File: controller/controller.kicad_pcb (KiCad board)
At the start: 4 copper layers, 30 x 60 mm, 74 parts, among them SW1 SW_SPDT, SW2 SW_SPST

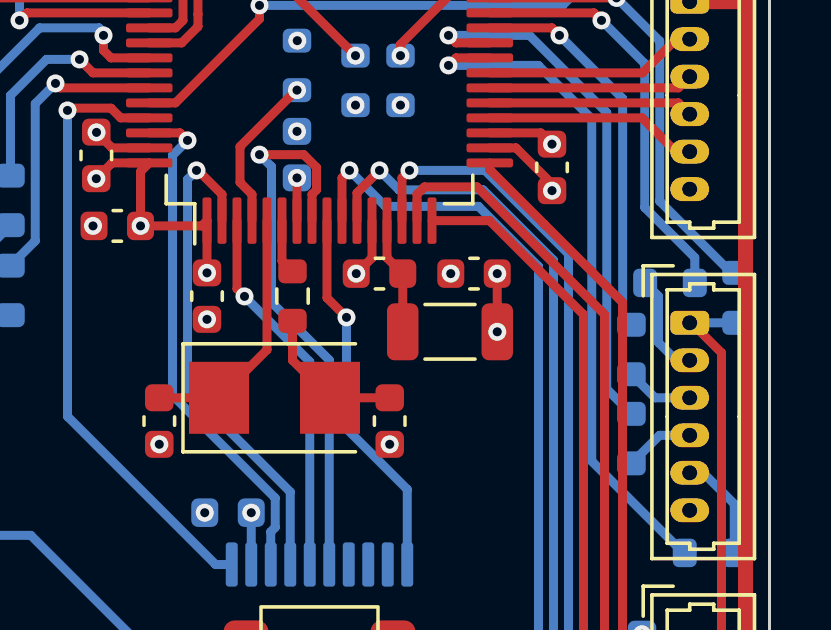
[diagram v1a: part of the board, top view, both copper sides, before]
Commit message: start work on host mcu
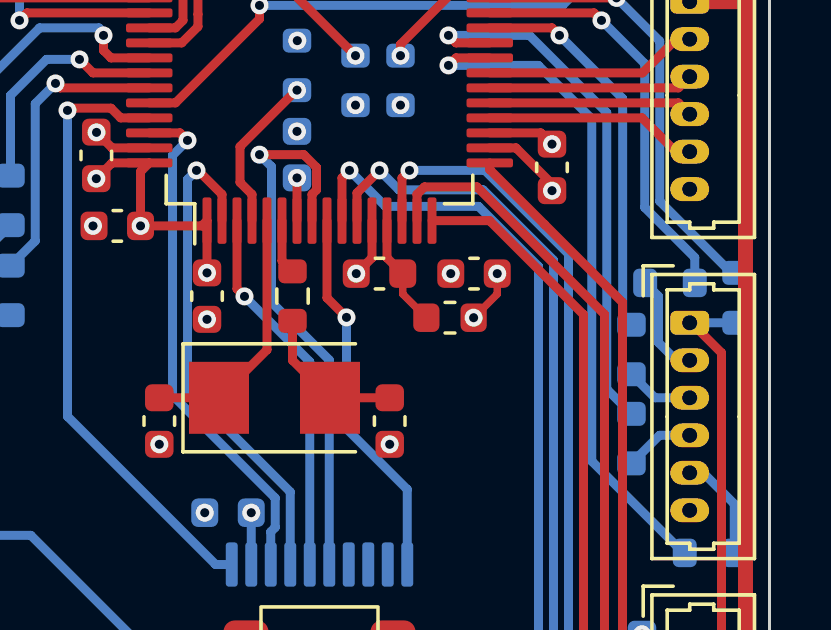
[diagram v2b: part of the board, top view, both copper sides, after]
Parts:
- FB1: footprint Inductor_SMD:L_1206_3216Metric -> Inductor_SMD:L_0603_1608Metric
- moved FB1 0.47 mm to (129.3, 79.9)
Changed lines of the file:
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@@
     )
   )
-  (footprint "Inductor_SMD:L_1206_3216Metric" (layer "F.Cu")
-    (at 129.35 80.38 180)
-    (descr "Inductor SMD 1206 (3216 Metric), square (rectangular) end terminal, IPC_7351 nominal, (Body size source: IPC-SM-782 page 80, https://www.pcb-3d.com/wordpress/wp-content/uploads/ipc-sm-782a_amendment_1_and_2.pdf), generated with kicad-footprint-generator")
+  (footprint "Inductor_SMD:L_0603_1608Metric" (layer "F.Cu")
+    (at 129.35 79.91 180)
+    (descr "Inductor SMD 0603 (1608 Metric), square (rectangular) end terminal, IPC_7351 nominal, (Body size source: http://www.tortai-tech.com/upload/download/2011102023233369053.pdf), generated with kicad-footprint-generator")
     (tags "inductor")
     (property "Sheetfile" "controller.kicad_sch")
     (property "Sheetname" "")
     (attr smd)
-    (fp_text reference "FB1" (at 0 -1.9) (layer "F.Fab")
+    (fp_text reference "FB1" (at 0 -1.43 180) (layer "F.Fab")
       (effects (font (size 1 1) (thickness 0.15)))
     )
-    (fp_text value "120R" (at 0 1.9) (layer "F.Fab")
+    (fp_text value "120R" (at 0 1.43 180) (layer "F.Fab")
       (effects (font (size 1 1) (thickness 0.15)))
     )
-    (fp_text user "${REFERENCE}" (at 0 0) (layer "F.Fab")
-      (effects (font (size 0.8 0.8) (thickness 0.12)))
+    (fp_text user "${REFERENCE}" (at 0 0 180) (layer "F.Fab")
+      (effects (font (size 0.4 0.4) (thickness 0.06)))
     )
-    (fp_line (start -0.835242 0.91) (end 0.835242 0.91) (layer "F.SilkS") (width 0.12))
-    (fp_line (start -0.835242 -0.91) (end 0.835242 -0.91) (layer "F.SilkS") (width 0.12))
-    (fp_line (start 2.35 -1.2) (end 2.35 1.2) (layer "F.CrtYd") (width 0.05))
-    (fp_line (start 2.35 1.2) (end -2.35 1.2) (layer "F.CrtYd") (width 0.05))
-    (fp_line (start -2.35 -1.2) (end 2.35 -1.2) (layer "F.CrtYd") (width 0.05))
-    (fp_line (start -2.35 1.2) (end -2.35 -1.2) (layer "F.CrtYd") (width 0.05))
-    (fp_line (start -1.6 0.8) (end -1.6 -0.8) (layer "F.Fab") (width 0.1))
-    (fp_line (start 1.6 0.8) (end -1.6 0.8) (layer "F.Fab") (width 0.1))
-    (fp_line (start -1.6 -0.8) (end 1.6 -0.8) (layer "F.Fab") (width 0.1))
-    (fp_line (start 1.6 -0.8) (end 1.6 0.8) (layer "F.Fab") (width 0.1))
-    (pad "1" smd roundrect (at -1.575 0 180) (size 1.05 1.9) (layers "F.Cu" "F.Paste" "F.Mask") (roundrect_rratio 0.238095)
+    (fp_line (start -0.162779 -0.51) (end 0.162779 -0.51) (layer "F.SilkS") (width 0.12))
+    (fp_line (start -0.162779 0.51) (end 0.162779 0.51) (layer "F.SilkS") (width 0.12))
+    (fp_line (start -1.48 -0.73) (end 1.48 -0.73) (layer "F.CrtYd") (width 0.05))
+    (fp_line (start 1.48 -0.73) (end 1.48 0.73) (layer "F.CrtYd") (width 0.05))
+    (fp_line (start 1.48 0.73) (end -1.48 0.73) (layer "F.CrtYd") (width 0.05))
+    (fp_line (start -1.48 0.73) (end -1.48 -0.73) (layer "F.CrtYd") (width 0.05))
+    (fp_line (start -0.8 0.4) (end -0.8 -0.4) (layer "F.Fab") (width 0.1))
+    (fp_line (start 0.8 -0.4) (end 0.8 0.4) (layer "F.Fab") (width 0.1))
+    (fp_line (start 0.8 0.4) (end -0.8 0.4) (layer "F.Fab") (width 0.1))
+    (fp_line (start -0.8 -0.4) (end 0.8 -0.4) (layer "F.Fab") (width 0.1))
+    (pad "1" smd roundrect (at -0.7875 0 180) (size 0.875 0.95) (layers "F.Cu" "F.Paste" "F.Mask") (roundrect_rratio 0.25)
       (net 3 "+3V3") (pintype "passive"))
-    (pad "2" smd roundrect (at 1.575 0 180) (size 1.05 1.9) (layers "F.Cu" "F.Paste" "F.Mask") (roundrect_rratio 0.238095)
+    (pad "2" smd roundrect (at 0.7875 0 180) (size 0.875 0.95) (layers "F.Cu" "F.Paste" "F.Mask") (roundrect_rratio 0.25)
       (net 4 "+3.3VA") (pintype "passive"))
-    (model "${KICAD6_3DMODEL_DIR}/Inductor_SMD.3dshapes/L_1206_3216Metric.wrl"
+    (model "${KICAD6_3DMODEL_DIR}/Inductor_SMD.3dshapes/L_0603_1608Metric.wrl"
       (offset (xyz 0 0 0))
       (scale (xyz 1 1 1))
@@
   (segment (start 131.915 67.25) (end 132.4325 66.7325) (width 0.3) (layer "F.Cu") (net 3))
   (segment (start 130.0375 60.05) (end 131 60.05) (width 0.3) (layer "F.Cu") (net 3))
+  (segment (start 130.925 78.44) (end 130.925 79.1225) (width 0.25) (layer "F.Cu") (net 3))
+  (segment (start 130.925 79.1225) (end 130.1375 79.91) (width 0.25) (layer "F.Cu") (net 3))
   (segment (start 119.035 75.04) (end 119.325 74.75) (width 0.3) (layer "F.Cu") (net 3))
   (segment (start 132.375 73.75) (end 132.7375 74.1125) (width 0.3) (layer "F.Cu") (net 3))
@@
   (segment (start 119.035 76.85) (end 119.035 75.04) (width 0.3) (layer "F.Cu") (net 3))
   (segment (start 121.25 76.675) (end 121.25 78.415) (width 0.3) (layer "F.Cu") (net 3))
-  (segment (start 130.925 79.475) (end 130.925 80.38) (width 0.3) (layer "F.Cu") (net 3))
   (segment (start 132.7375 74.1125) (end 132.75 74.125) (width 0.3) (layer "F.Cu") (net 3))
-  (segment (start 130.925 78.44) (end 130.925 79.475) (width 0.3) (layer "F.Cu") (net 3))
   (segment (start 121.25 65.325) (end 120.4 65.325) (width 0.3) (layer "F.Cu") (net 3))
   (via (at 121.25 78.415) (size 0.6) (drill 0.3) (layers "F.Cu" "B.Cu") (net 3))
@@
   (via (at 119.035 76.85) (size 0.6) (drill 0.3) (layers "F.Cu" "B.Cu") (net 3))
   (via (at 131.76 60.05) (size 0.6) (drill 0.3) (layers "F.Cu" "B.Cu") (net 3))
-  (via (at 130.925 80.38) (size 0.6) (drill 0.3) (layers "F.Cu" "B.Cu") (net 3))
+  (via (at 130.1375 79.91) (size 0.6) (drill 0.3) (layers "F.Cu" "B.Cu") (net 3))
   (via (at 132.44 66.725) (size 0.6) (drill 0.3) (layers "F.Cu" "B.Cu") (net 3))
   (via (at 117.56 75.275) (size 0.6) (drill 0.3) (layers "F.Cu" "B.Cu") (net 3))
@@
   (segment (start 127.25 77.915) (end 127.775 78.44) (width 0.3) (layer "F.Cu") (net 4))
   (segment (start 127.25 76.675) (end 127.25 77.915) (width 0.3) (layer "F.Cu") (net 4))
-  (segment (start 127.775 78.44) (end 127.775 80.38) (width 0.3) (layer "F.Cu") (net 4))
+  (segment (start 127.775 78.44) (end 127.775 79.1225) (width 0.25) (layer "F.Cu") (net 4))
+  (segment (start 127.775 79.1225) (end 128.5625 79.91) (width 0.25) (layer "F.Cu") (net 4))
   (segment (start 130.675 68.25) (end 129.25 68.25) (width 0.3) (layer "F.Cu") (net 5))
   (via (at 129.25 68.25) (size 0.6) (drill 0.3) (layers "F.Cu" "B.Cu") (net 5))

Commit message: update controller and host boards
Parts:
- removed ESD1: USBLC6-2SC6, Package_TO_SOT_SMD:SOT-23-6
- removed H10, H11, H12, H13, H14: Conn_01x03, Connector_Molex:Molex_PicoBlade_53047-0310_1x03_P1.25mm_Vertical
- removed H2, H4, H5, H6: Conn_01x06, Connector_Molex:Molex_PicoBlade_53047-0610_1x06_P1.25mm_Vertical
- removed H3, H8, H9: Conn_01x05, Connector_Molex:Molex_PicoBlade_53047-0510_1x05_P1.25mm_Vertical
- removed H7: Conn_01x04, Connector_Molex:Molex_PicoBlade_53047-0410_1x04_P1.25mm_Vertical
- removed LDO1: AP2127N-3.3, Package_TO_SOT_SMD:SOT-23
- removed MCU1: STM32F401RCT6, Package_QFP:LQFP-64_10x10mm_P0.5mm
- removed MNT1: MountingHole, MountingHole:MountingHole_2.2mm_M2_Pad
- removed R10, R11, R12, R13, R14, R15, R16, R17, R18, R19, R20, R21, R22, R23, R24, R25, R26, R27, R28, R29, R5, R6, R7, R8, R9: 10KR, Resistor_SMD:R_0603_1608Metric
- removed SW2: SW_SPST, Custom:ALPS_SKRKAEE020
- removed USB1: USB_A, Custom:JST_UBA-4R-D14T-4D
- removed VT1: TXS0108EPW, Package_SO:TSSOP-20_4.4x6.5mm_P0.65mm
- removed XTAL1: 8MHz, Crystal:Crystal_SMD_5032-2Pin_5.0x3.2mm
- added J1: Conn_01x02, klib:MOLEX_533750210-Mini-Lock-2Pin-Through-Hole, F.Cu at (135.7, 74.0)
- added J10: Conn_01x05, Connector_Molex:Molex_PicoBlade_53047-0510_1x05_P1.25mm_Vertical, F.Cu at (137.3, 107.5)
- added J11: Conn_01x02, klib:MOLEX_533750210-Mini-Lock-2Pin-Through-Hole, F.Cu at (135.7, 126.0)
- added J2: USB_C_Receptacle_USB2.0, Connector_USB:USB_C_Receptacle_HRO_TYPE-C-31-M-12, F.Cu at (125.0, 73.0)
- added J3: Conn_01x02, klib:MOLEX_533750210-Mini-Lock-2Pin-Through-Hole, F.Cu at (114.3, 126.0)
- added J4: Conn_01x05, Connector_Molex:Molex_PicoBlade_53047-0510_1x05_P1.25mm_Vertical, F.Cu at (127.5, 127.3)
- added J5: Conn_01x04, Connector_Molex:Molex_PicoBlade_53047-0410_1x04_P1.25mm_Vertical, F.Cu at (112.7, 94.5)
- added J6: Conn_01x04, Connector_Molex:Molex_PicoBlade_53047-0410_1x04_P1.25mm_Vertical, F.Cu at (137.3, 92.5)
- added J7: Conn_01x05, Connector_Molex:Molex_PicoBlade_53047-0510_1x05_P1.25mm_Vertical, F.Cu at (112.7, 85.8)
- added J8: Conn_01x05, Connector_Molex:Molex_PicoBlade_53047-0510_1x05_P1.25mm_Vertical, F.Cu at (137.3, 82.5)
- added J9: Conn_01x05, Connector_Molex:Molex_PicoBlade_53047-0510_1x05_P1.25mm_Vertical, F.Cu at (112.7, 110.8)
- added U1: AP2127N-3.3, Package_TO_SOT_SMD:SOT-23, F.Cu at (131.2, 81.2)
- added U2: STM32F401RCT6, Package_QFP:LQFP-64_10x10mm_P0.5mm, F.Cu at (125.0, 94.0)
- added U3: USBLC6-2SC6, Package_TO_SOT_SMD:SOT-23-6, F.Cu at (123.0, 82.0)
- added U4: TXS0108EPW, Package_SO:TSSOP-20_4.4x6.5mm_P0.65mm, F.Cu at (125.0, 120.0)
- added Y1: 8M, Crystal:Crystal_SMD_5032-2Pin_5.0x3.2mm, F.Cu at (123.5, 106.5)
- C1, C2, C3, C9: value 10uF -> 10u
- C10, C4, C5, C6, C7, C8: value 100nF -> 100n
- C11: value 4.7uF -> 20p; moved to F.Cu
- C12: value 100nF -> 20p; moved to F.Cu
- C13: value 20pF -> 4.7u
- C14: value 20pF -> 100n
- C15, C16, C17, C18, C19, C20, C21: value 100nF -> 100n; moved to F.Cu
- H1: value Conn_01x06 -> MountingHole; footprint Connector_Molex:Molex_PicoBlade_53047-0610_1x06_P1.25mm_Vertical -> MountingHole:MountingHole_2.2mm_M2_Pad
- R1: value 0R -> 0
- R2, R3, R4: value 10KR -> 10K; moved to F.Cu
- SW1: footprint Custom:ALPS_SSSS912000 -> klib:ALPS_SSSS912000
- moved SW1 65.4 mm to (125.0, 113.0), turned to 180 degrees
- moved R4 53.4 mm to (134.8, 112.5)
- moved R2 44.7 mm to (125.0, 109.5), turned to 180 degrees
- moved C11 38.1 mm to (119.5, 105.3), turned to 90 degrees
- moved C15 33.0 mm to (119.5, 120.0), turned to 180 degrees
- moved C12 31.0 mm to (127.4, 105.3), turned to 90 degrees
- moved C16 26.2 mm to (130.5, 120.0), turned to 0 degrees
- moved C20 24.7 mm to (134.8, 107.5), turned to 90 degrees
- moved C9 23.8 mm to (130.4, 102.2), turned to 90 degrees
- moved R1 23.8 mm to (124.2, 103.0), turned to -90 degrees
- moved H1 23.8 mm to (114.0, 74.0), turned to 0 degrees
- moved FB1 23.1 mm to (128.1, 103.0)
- moved C5 23.1 mm to (132.5, 98.0)
- moved C10 23.1 mm to (128.1, 101.5), turned to 0 degrees
- moved C17 23.1 mm to (115.2, 105.8), turned to 90 degrees
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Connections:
- net +3.3VA renamed VREF
- C1 pad 1: VBUS -> 5V
- C11 pad 1: VCAP -> HSE_IN
- C12 pad 1: GND -> Net-(C12-Pad1)
- C12 pad 2: NRST -> GND
- C13 pad 1: HSE_IN -> VCAP
- C14 pad 1: Net-(C14-Pad1) -> NRST
- C15 pad 1: ST_X -> 3V3
- C16 pad 1: ST_Y -> 5V
- C2 pad 1: +3V3 -> 3V3
- C20 pad 1: GND -> ST_X
- C20 pad 2: +3V3 -> GND
- C21 pad 1: GND -> ST_Y
- C21 pad 2: VBUS -> GND
- C3 pad 1: +3V3 -> 3V3
- C4 pad 1: +3V3 -> 3V3
- C5 pad 1: +3V3 -> 3V3
- C6 pad 1: +3V3 -> 3V3
- C7 pad 1: +3V3 -> 3V3
- C8 pad 1: +3V3 -> 3V3
- C9 pad 1: +3V3 -> 3V3
- FB1 pad 1: +3V3 -> 3V3
- H1 pad 1: VBUS -> (no net)
- R1 pad 1: Net-(C14-Pad1) -> HSE_OUT
- R1 pad 2: HSE_OUT -> Net-(C12-Pad1)
- R2 pad 1: BOOT0 -> Net-(R2-Pad1)
- R2 pad 2: Net-(R2-Pad2) -> BOOT0
- R3 pad 1: BOOT1/KR1 -> BOOT1
- R3 pad 2: KR1 -> GND
- R4 pad 1: KT1 -> ST_P_IN
- R4 pad 2: KT1_IN -> ST_P
- SW1 pad 2: Net-(R2-Pad2) -> Net-(R2-Pad1)
- SW1 pad 3: +3V3 -> 3V3
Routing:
- net 5V: track 0.00 -> 145.5 mm, vias 0 -> 2
- net VBUS: track 131.6 -> 0.00 mm, vias 1 -> 0
- net 3V3: track 0.00 -> 70.4 mm, vias 0 -> 21
- net KR1: track 31.7 -> 0.00 mm
- net KI5: track 27.9 -> 0.00 mm, vias 1 -> 0
- net GND: track 12.6 -> 38.7 mm, vias 29 -> 33
- net KI1: track 26.1 -> 0.00 mm, vias 1 -> 0
- net LED4: track 12.5 -> 38.3 mm, vias 1 -> 2
- net KI2: track 24.8 -> 0.00 mm, vias 1 -> 0
- net KI4: track 23.3 -> 0.00 mm, vias 1 -> 0
- net KR5: track 22.8 -> 0.00 mm, vias 1 -> 0
- net KI3: track 22.4 -> 0.00 mm, vias 1 -> 0
- net LED_OE: track 12.6 -> 34.1 mm, vias 1 -> 2
- net COL1: track 0.00 -> 19.0 mm, vias 0 -> 1
- net +3V3: track 18.9 -> 0.00 mm, vias 12 -> 0
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- added copper zone on In2.Cu, net 3V3
- removed copper zone on In2.Cu, net +3V3
